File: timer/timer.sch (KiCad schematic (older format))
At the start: 3 parts, among them P1 CONN_01X05, U1 74HC02, U2 74HC27

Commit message: More of page 1 of the timer module (poorly drawn)
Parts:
- removed P1: CONN_01X05, symbol CONN_01X05
- added P1: CONN_01X12, symbol CONN_01X12
- added U3, U5: 74HC04, symbol 74HC04
- added U4: 74HC02, symbol 74HC02
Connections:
- net labels added: CT, CT/, PHS2, PHS2/, PHS4, PHS4/, RT, TT/, WT, WT/, cdiv1_a, cdiv1_b, cdiv1_d
- wire segments 38 -> 72

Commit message: Fleshed out the rest of page 1 of the timer module
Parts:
- removed P1: CONN_01X12, symbol CONN_01X12
- added P1: CONN_01X20, symbol CONN_01X20
- added unit 2 of U4
- added unit 4 of U5
- added unit 5 of U5
- added unit 6 of U5
- added U6, U9: 74HC02, symbol 74HC02
- added U7: 74HC27, symbol 74HC27
- added unit 1 of U8
- added unit 3 of U8
- added unit 4 of U8
- added unit 2 of U8
- added unit 5 of U8
- renumbered U5 to U8
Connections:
- net labels added: EVNSET, EVNSET/, ODDSET/, OVFSTB/, RINGA/, RINGB/, STOP, cdiv2_a, cdiv2_b, cdiv2_c, cdiv2_d, cdiv2_fs, cdiv2_fs/, oddset, ovfstb_r1, ovfstb_r2, ovfstb_r3, ovfstb_r4, ovfstb_r5, ovfstb_r6
- wire segments 72 -> 158
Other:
- moved on the sheet: U1A, U1B, U1C, U1D, U2A, U2B, U3A, U3B, U3C, U3D, U3E, U3F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

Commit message: Added PHS3/ from A24-2 since it makes more sense in the timer modules, along with the two monitor signals on A2-1, and an inverter and signal I missed
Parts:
- added U10: 74HC04, symbol 74HC04
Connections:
- net labels added: CLK, MONWT, PHS3/, Q2A
- wire segments 158 -> 165
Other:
- note added: "Combine these?"
- note added: "Moved from A24-2"
- moved on the sheet: U3D, U3E, U3F, U5B, U5C
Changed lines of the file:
@@
 L 74HC04 U3
 U 4 1 561AE65B
-P 3100 4950
-F 0 "U3" H 3250 5050 40  0000 C CNN
-F 1 "74HC04" H 3300 4850 40  0000 C CNN
-F 2 "" H 3100 4950 60  0000 C CNN
-F 3 "" H 3100 4950 60  0000 C CNN
-	4    3100 4950
+P 3050 5100
+F 0 "U3" H 3200 5200 40  0000 C CNN
+F 1 "74HC04" H 3250 5000 40  0000 C CNN
+F 2 "" H 3050 5100 60  0000 C CNN
+F 3 "" H 3050 5100 60  0000 C CNN
+	4    3050 5100
 	1    0    0    -1
 $EndComp
@@
 L 74HC04 U3
 U 5 1 561AE708
-P 4050 4950
-F 0 "U3" H 4200 5050 40  0000 C CNN
-F 1 "74HC04" H 4250 4850 40  0000 C CNN
-F 2 "" H 4050 4950 60  0000 C CNN
-F 3 "" H 4050 4950 60  0000 C CNN
-	5    4050 4950
+P 3850 5100
+F 0 "U3" H 4000 5200 40  0000 C CNN
+F 1 "74HC04" H 4050 5000 40  0000 C CNN
+F 2 "" H 3850 5100 60  0000 C CNN
+F 3 "" H 3850 5100 60  0000 C CNN
+	5    3850 5100
 	1    0    0    -1
 $EndComp
@@
 L 74HC04 U3
 U 6 1 561AE781
-P 5000 4950
-F 0 "U3" H 5150 5050 40  0000 C CNN
-F 1 "74HC04" H 5200 4850 40  0000 C CNN
-F 2 "" H 5000 4950 60  0000 C CNN
-F 3 "" H 5000 4950 60  0000 C CNN
-	6    5000 4950
-	1    0    0    -1
-$EndComp
-Text GLabel 4600 5100 2    60   Input ~ 0
+P 4900 5100
+F 0 "U3" H 5050 5200 40  0000 C CNN
+F 1 "74HC04" H 5100 5000 40  0000 C CNN
+F 2 "" H 4900 5100 60  0000 C CNN
+F 3 "" H 4900 5100 60  0000 C CNN
+	6    4900 5100
+	1    0    0    -1
+$EndComp
+Text GLabel 4500 5250 2    60   Input ~ 0
 CT
-Text GLabel 5550 4950 2    60   Input ~ 0
+Text GLabel 5450 5400 2    60   Input ~ 0
 CT/
 Text GLabel 5900 650  2    60   Input ~ 0
@@
 L 74HC04 U5
 U 2 1 561AF566
-P 6550 4550
-F 0 "U5" H 6700 4650 40  0000 C CNN
-F 1 "74HC04" H 6750 4450 40  0000 C CNN
-F 2 "" H 6550 4550 60  0000 C CNN
-F 3 "" H 6550 4550 60  0000 C CNN
-	2    6550 4550
+P 7850 4550
+F 0 "U5" H 8000 4650 40  0000 C CNN
+F 1 "74HC04" H 8050 4450 40  0000 C CNN
+F 2 "" H 7850 4550 60  0000 C CNN
+F 3 "" H 7850 4550 60  0000 C CNN
+	2    7850 4550
 	1    0    0    -1
 $EndComp
@@
 L 74HC04 U5
 U 3 1 561AF5FF
-P 6550 4950
-F 0 "U5" H 6700 5050 40  0000 C CNN
-F 1 "74HC04" H 6750 4850 40  0000 C CNN
-F 2 "" H 6550 4950 60  0000 C CNN
-F 3 "" H 6550 4950 60  0000 C CNN
-	3    6550 4950
+P 7850 4950
+F 0 "U5" H 8000 5050 40  0000 C CNN
+F 1 "74HC04" H 8050 4850 40  0000 C CNN
+F 2 "" H 7850 4950 60  0000 C CNN
+F 3 "" H 7850 4950 60  0000 C CNN
+	3    7850 4950
 	1    0    0    -1
 $EndComp
@@
 Connection ~ 2750 4200
 Wire Wire Line
-	2600 2250 2600 4950
-Wire Wire Line
-	2600 4950 2650 4950
+	2600 2250 2600 5100
 Connection ~ 2600 2250
 Wire Wire Line
-	4500 4950 4550 4950
-Wire Wire Line
-	3550 4950 3600 4950
-Wire Wire Line
-	4550 4950 4550 5100
-Wire Wire Line
-	4550 5100 4600 5100
-Connection ~ 4550 4950
-Wire Wire Line
-	5450 4950 5550 4950
+	4300 5100 4450 5100
+Wire Wire Line
+	3500 5100 3400 5100
+Wire Wire Line
+	4450 4850 4450 5250
+Wire Wire Line
+	4450 5250 4500 5250
+Connection ~ 4450 5100
 Wire Wire Line
 	6700 1000 6800 1000
@@
 Connection ~ 5750 1000
 Wire Wire Line
-	5400 4550 6100 4550
-Wire Wire Line
-	6100 4550 6100 5250
-Text GLabel 6200 5250 2    60   Input ~ 0
+	5400 4550 7400 4550
+Wire Wire Line
+	7400 4550 7400 5250
+Text GLabel 7500 5250 2    60   Input ~ 0
 WT
 Wire Wire Line
-	6100 5250 6200 5250
-Connection ~ 6100 4950
-Text GLabel 7100 4950 2    60   Input ~ 0
+	7400 5250 7500 5250
+Connection ~ 7400 4950
+Text GLabel 8400 4950 2    60   Input ~ 0
 TT/
-Text GLabel 7100 4550 2    60   Input ~ 0
+Text GLabel 8550 4550 2    60   Input ~ 0
 WT/
 Wire Wire Line
-	7000 4550 7100 4550
-Wire Wire Line
-	7000 4950 7100 4950
+	8300 4950 8400 4950
 Text GLabel 10500 1900 0    60   Input ~ 0
 PHS2
@@
 	2700 5550 2700 5850
 Wire Wire Line
-	5500 4950 5500 5400
-Wire Wire Line
-	5500 5400 1400 5400
+	5400 5100 5400 5400
+Wire Wire Line
+	1400 5400 5450 5400
 Wire Wire Line
 	1400 5400 1400 5850
-Connection ~ 5500 4950
 Text Label 2600 5950 0    60   ~ 0
 ovfstb_r1
@@
 Text Label 8850 1550 0    60   ~ 0
 oddset
+$Comp
+L 74HC04 U10
+U 1 1 561CD62B
+P 5850 4850
+F 0 "U10" H 6000 4950 40  0000 C CNN
+F 1 "74HC04" H 6050 4750 40  0000 C CNN
+F 2 "" H 5850 4850 60  0000 C CNN
+F 3 "" H 5850 4850 60  0000 C CNN
+	1    5850 4850
+	1    0    0    -1
+$EndComp
+Connection ~ 5400 5400
+Text GLabel 6450 4850 2    60   Input ~ 0
+PHS3/
+Wire Wire Line
+	6300 4850 6450 4850
+Text Notes 6800 5050 2    60   ~ 0
+Moved from A24-2
+Text Notes 8050 4350 2    60   ~ 0
+Combine these?
+$Comp
+L 74HC04 U10
+U 2 1 561D58A1
+P 9350 4750
+F 0 "U10" H 9500 4850 40  0000 C CNN
+F 1 "74HC04" H 9550 4650 40  0000 C CNN
+F 2 "" H 9350 4750 60  0000 C CNN
+F 3 "" H 9350 4750 60  0000 C CNN
+	2    9350 4750
+	1    0    0    -1
+$EndComp
+$Comp
+L 74HC04 U10
+U 3 1 561D59AF
+P 9350 4350
+F 0 "U10" H 9500 4450 40  0000 C CNN
+F 1 "74HC04" H 9550 4250 40  0000 C CNN
+F 2 "" H 9350 4350 60  0000 C CNN
+F 3 "" H 9350 4350 60  0000 C CNN
+	3    9350 4350
+	1    0    0    -1
+$EndComp
+$Comp
+L 74HC04 U10
+U 4 1 561D633D
+P 9350 5150
+F 0 "U10" H 9500 5250 40  0000 C CNN
+F 1 "74HC04" H 9550 5050 40  0000 C CNN
+F 2 "" H 9350 5150 60  0000 C CNN
+F 3 "" H 9350 5150 60  0000 C CNN
+	4    9350 5150
+	1    0    0    -1
+$EndComp
+Wire Wire Line
+	8300 4550 8550 4550
+Wire Wire Line
+	8900 4350 8900 5150
+Connection ~ 8900 4750
+Wire Wire Line
+	8900 4750 8450 4750
+Wire Wire Line
+	8450 4750 8450 4550
+Connection ~ 8450 4550
+Text GLabel 9900 4350 2    60   Input ~ 0
+MONWT
+Wire Wire Line
+	9800 4350 9900 4350
+Text GLabel 9900 4750 2    60   Input ~ 0
+CLK
+Wire Wire Line
+	9800 4750 9900 4750
+Text GLabel 9900 5150 2    60   Input ~ 0
+Q2A
+Wire Wire Line
+	9800 5150 9900 5150
+Wire Wire Line
+	5350 5100 5400 5100
+Wire Wire Line
+	5400 4850 4450 4850
 $EndSCHEMATC

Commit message: Pushed page A02-1 down into a heirarchical sheet, while retaining the P1 connector at the top level. Also added the beginnings of page A02-2. The four-phase clock divider is now also on its own page, for ease of use.
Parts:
- removed P1: CONN_01X20, symbol CONN_01X20
- removed U1, U4, U6, U9: 74HC02, symbol 74HC02
- removed U10, U3, U5, U8: 74HC04, symbol 74HC04
- removed U2, U7: 74HC27, symbol 74HC27
- added P1: CONN_01X32, symbol CONN_01X32
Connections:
- net labels added: P01, P01/, P02, P02/, P03, P03/, P04, P04/, P05, P05/, RT/
- net labels removed: EVNSET, EVNSET/, MONWT, ODDSET/, Q2A, RINGA/, RINGB/, cdiv1_a, cdiv1_b, cdiv1_d, cdiv2_a, cdiv2_b, cdiv2_c, cdiv2_d, cdiv2_fs, cdiv2_fs/, oddset, ovfstb_r1, ovfstb_r2, ovfstb_r3, ovfstb_r4, ovfstb_r5, ovfstb_r6
- wire segments 165 -> 70
- no-connect marks 0 -> 4
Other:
- note removed: "Combine these?"
- note removed: "Moved from A24-2"

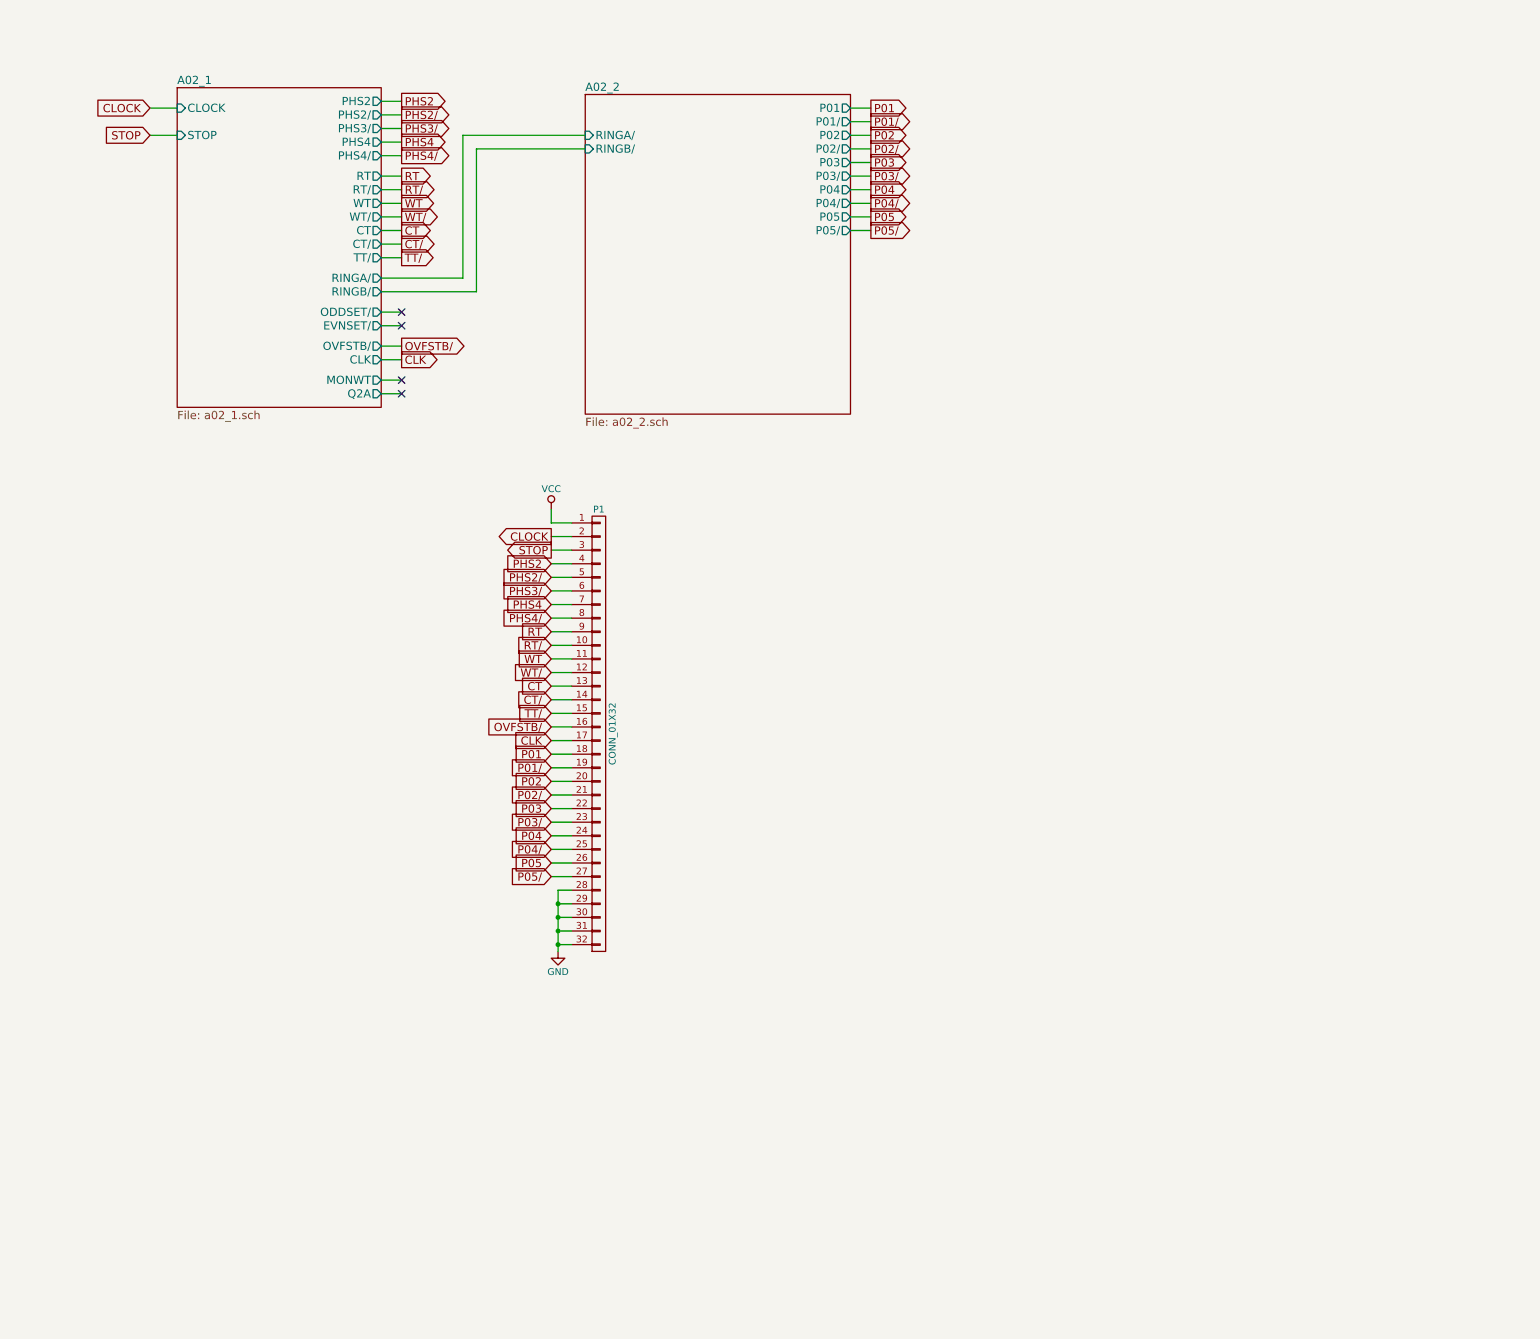
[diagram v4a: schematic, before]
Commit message: Added the start/stop logic to timer page A02-2, and introduced a new part, 74LVC07, that I think will be the solution for open drain things
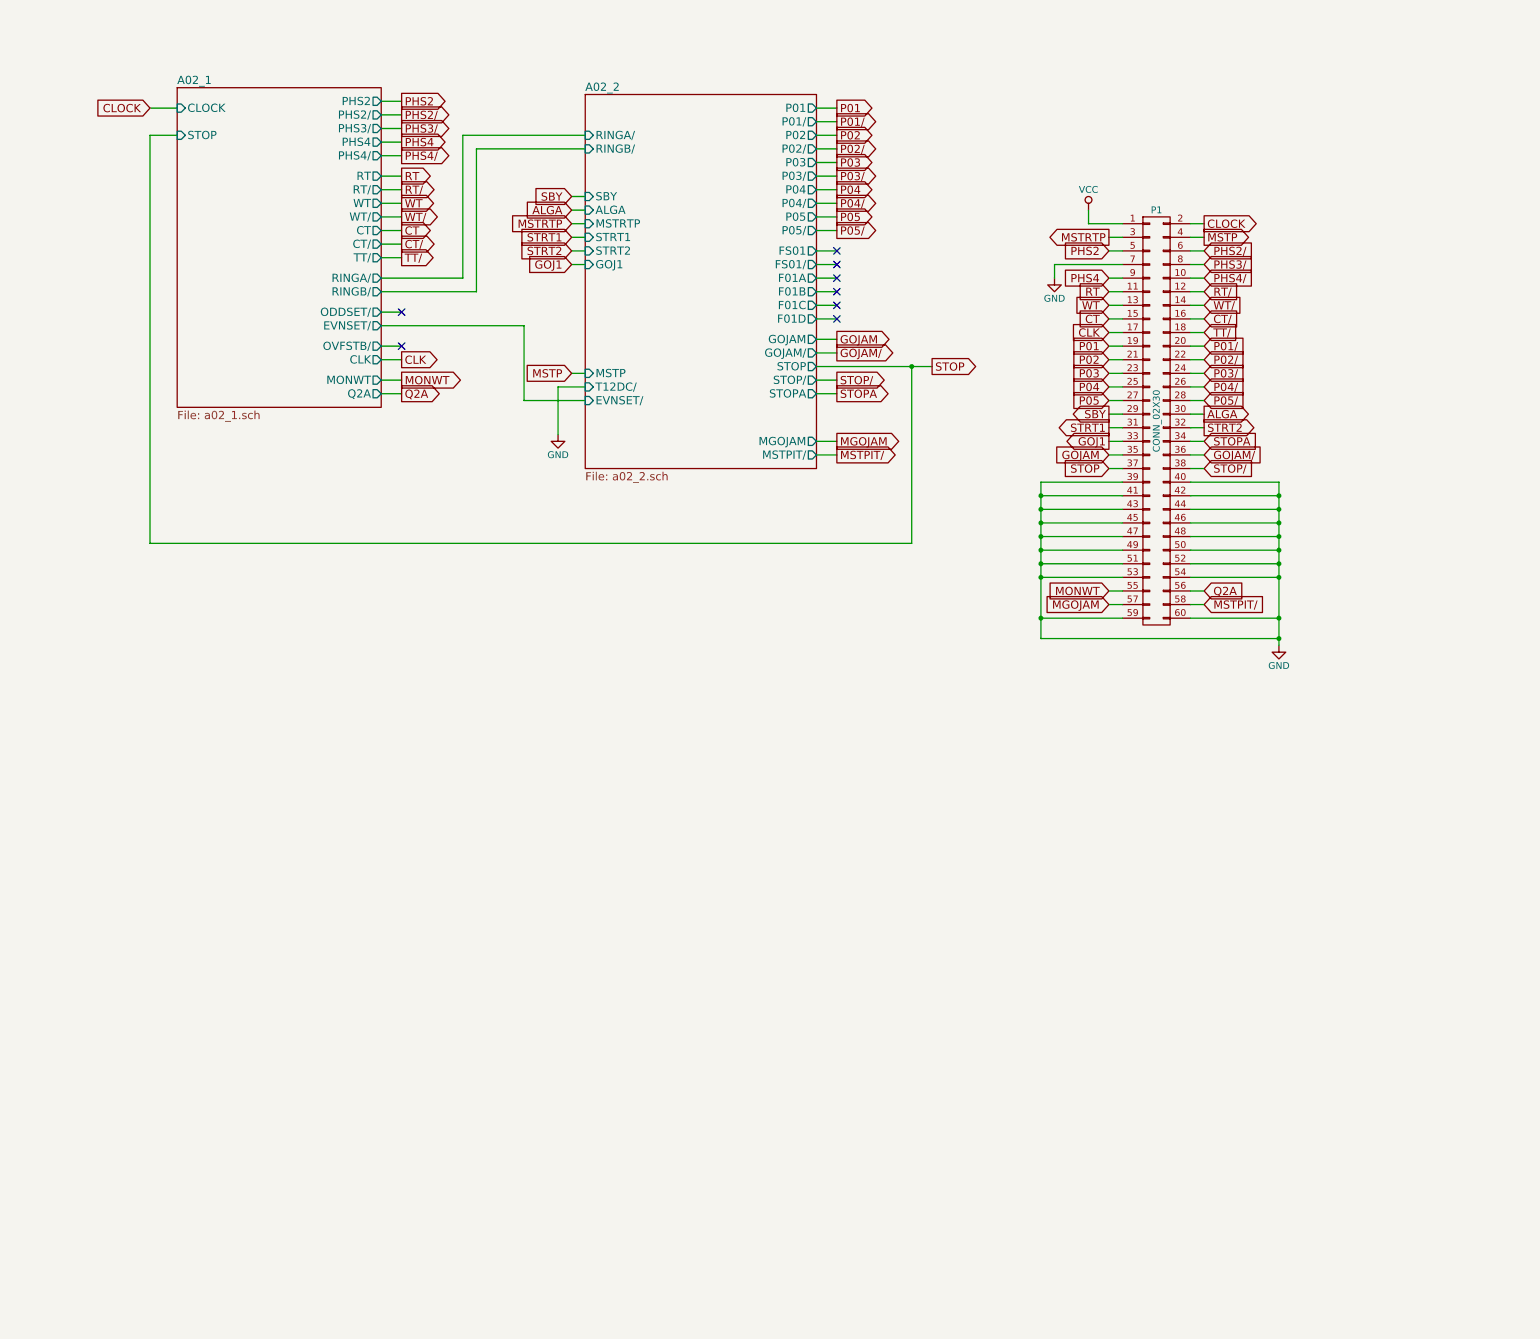
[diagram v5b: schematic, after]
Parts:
- removed P1: CONN_01X32, symbol CONN_01X32
- added P1: CONN_02X30, symbol CONN_02X30
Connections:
- net CLK: now also P1.17 (P17)
- net CLOCK: now also P1.2 (P2)
- net CT: now also P1.15 (P15)
- net CT/: now also P1.16 (P16)
- net GND: now also P1.39 (P39), P1.40 (P40), P1.41 (P41), P1.42 (P42), P1.43 (P43), P1.44 (P44), P1.45 (P45), P1.46 (P46), P1.47 (P47), P1.48 (P48), P1.49 (P49), P1.50 (P50), P1.51 (P51), P1.52 (P52), P1.53 (P53), P1.54 (P54), P1.59 (P59), P1.60 (P60), P1.7 (P7)
- net P01: now also P1.19 (P19)
- net P01/: now also P1.20 (P20)
- net P02: now also P1.21 (P21)
- net P02/: now also P1.22 (P22)
- net P03: now also P1.23 (P23)
- net P03/: now also P1.24 (P24)
- net P04: now also P1.25 (P25)
- net P04/: now also P1.26 (P26)
- net P05: now also P1.27 (P27)
- net P05/: now also P1.28 (P28)
- net PHS2: now also P1.5 (P5)
- net PHS2/: now also P1.6 (P6)
- net PHS3/: now also P1.8 (P8)
- net PHS4: now also P1.9 (P9)
- net PHS4/: now also P1.10 (P10)
- net RT: now also P1.11 (P11)
- net RT/: now also P1.12 (P12)
- net STOP: now also P1.37 (P37)
- net TT/: now also P1.18 (P18)
- net VCC: now also P1.1 (P1)
- net WT: now also P1.13 (P13)
- net WT/: now also P1.14 (P14)
- new net ALGA: P1.30 (P30)
- new net GOJ1: P1.33 (P33)
- new net GOJAM: P1.35 (P35)
- new net GOJAM/: P1.36 (P36)
- new net MGOJAM: P1.57 (P57)
- new net MONWT: P1.55 (P55)
- new net MSTP: P1.4 (P4)
- new net MSTPIT/: P1.58 (P58)
- new net MSTRTP: P1.3 (P3)
- new net Q2A: P1.56 (P56)
- new net SBY: P1.29 (P29)
- new net STOP/: P1.38 (P38)
- new net STOPA: P1.34 (P34)
- new net STRT1: P1.31 (P31)
- new net STRT2: P1.32 (P32)
- no-connect marks 4 -> 8

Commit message: Added the final page of the timer module. Leaving top-level wiring pretty bare for now until I have a better idea of what's needed outside the module.
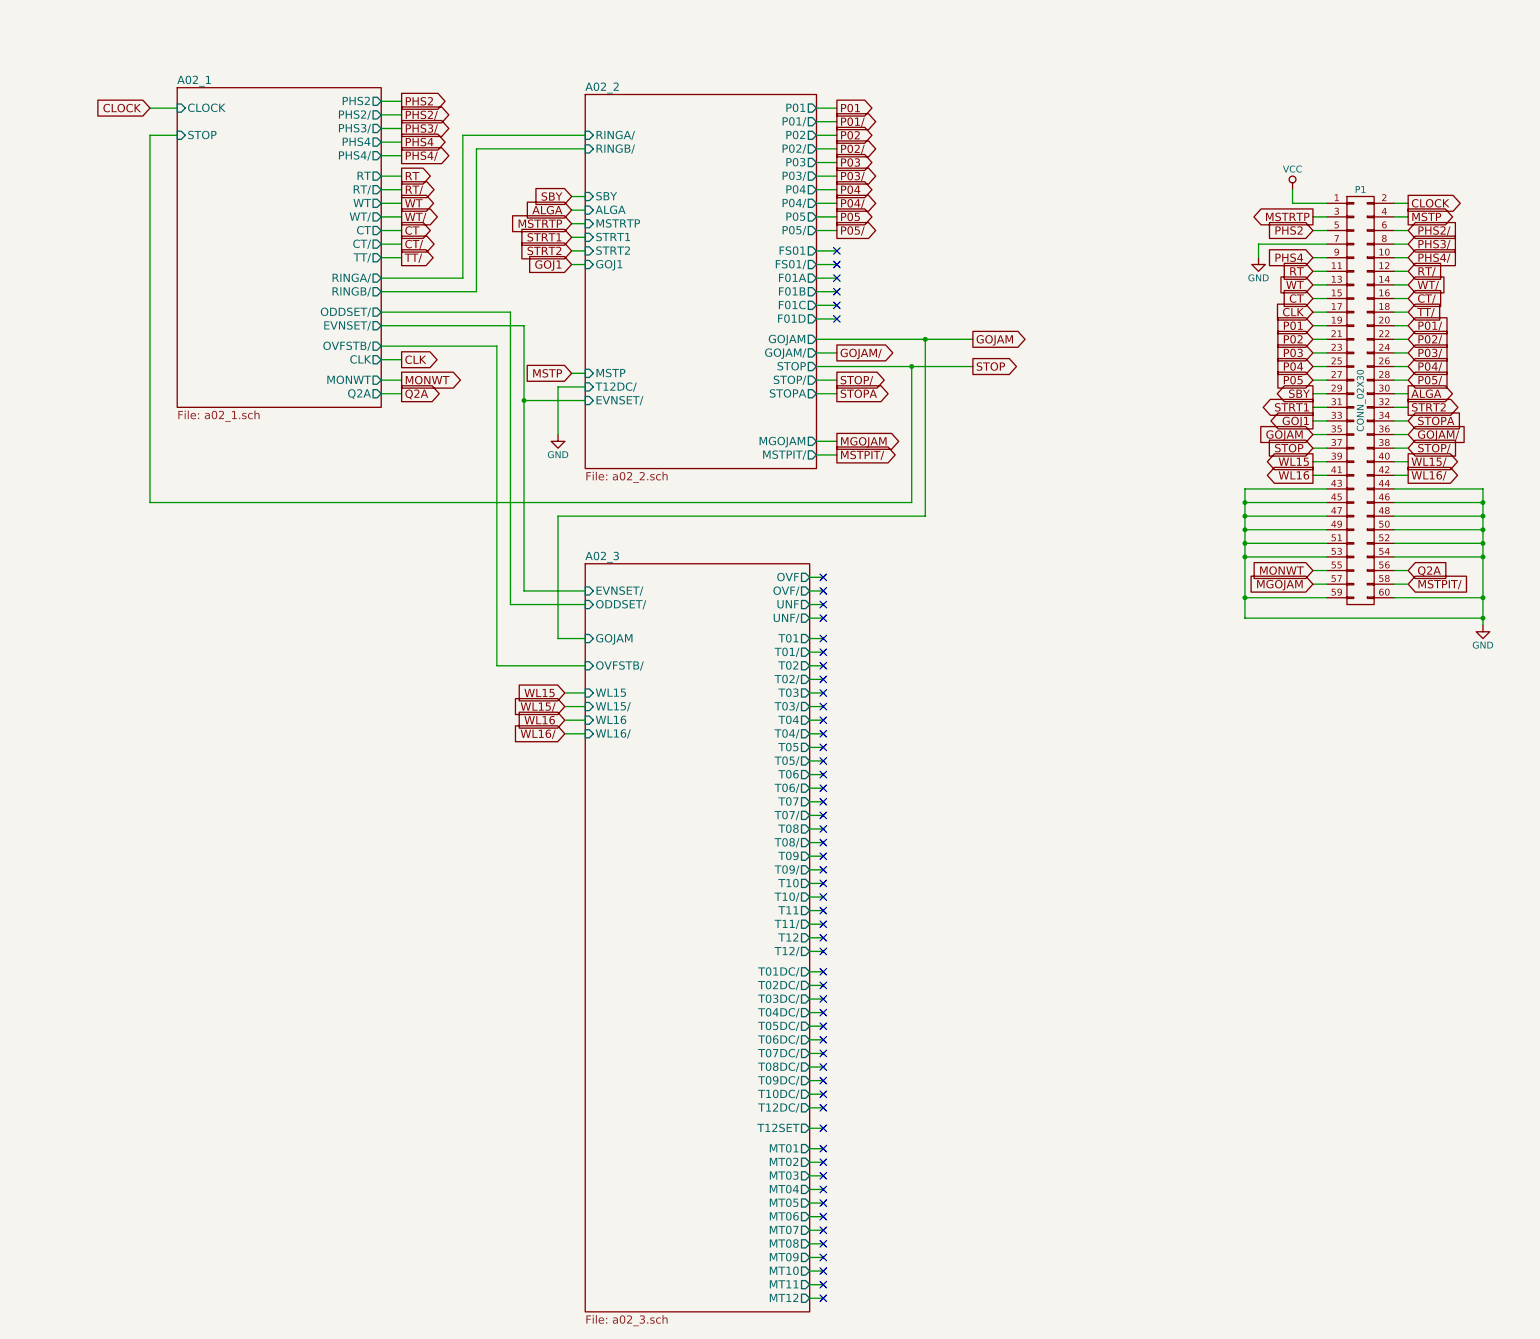
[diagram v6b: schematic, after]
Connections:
- net GND: no longer P1.39 (P39), P1.40 (P40), P1.41 (P41), P1.42 (P42)
- new net WL15: P1.39 (P39)
- new net WL15/: P1.40 (P40)
- new net WL16: P1.41 (P41)
- new net WL16/: P1.42 (P42)
- no-connect marks 8 -> 58
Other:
- moved on the sheet: P1
